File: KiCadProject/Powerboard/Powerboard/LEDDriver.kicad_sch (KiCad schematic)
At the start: 18 parts

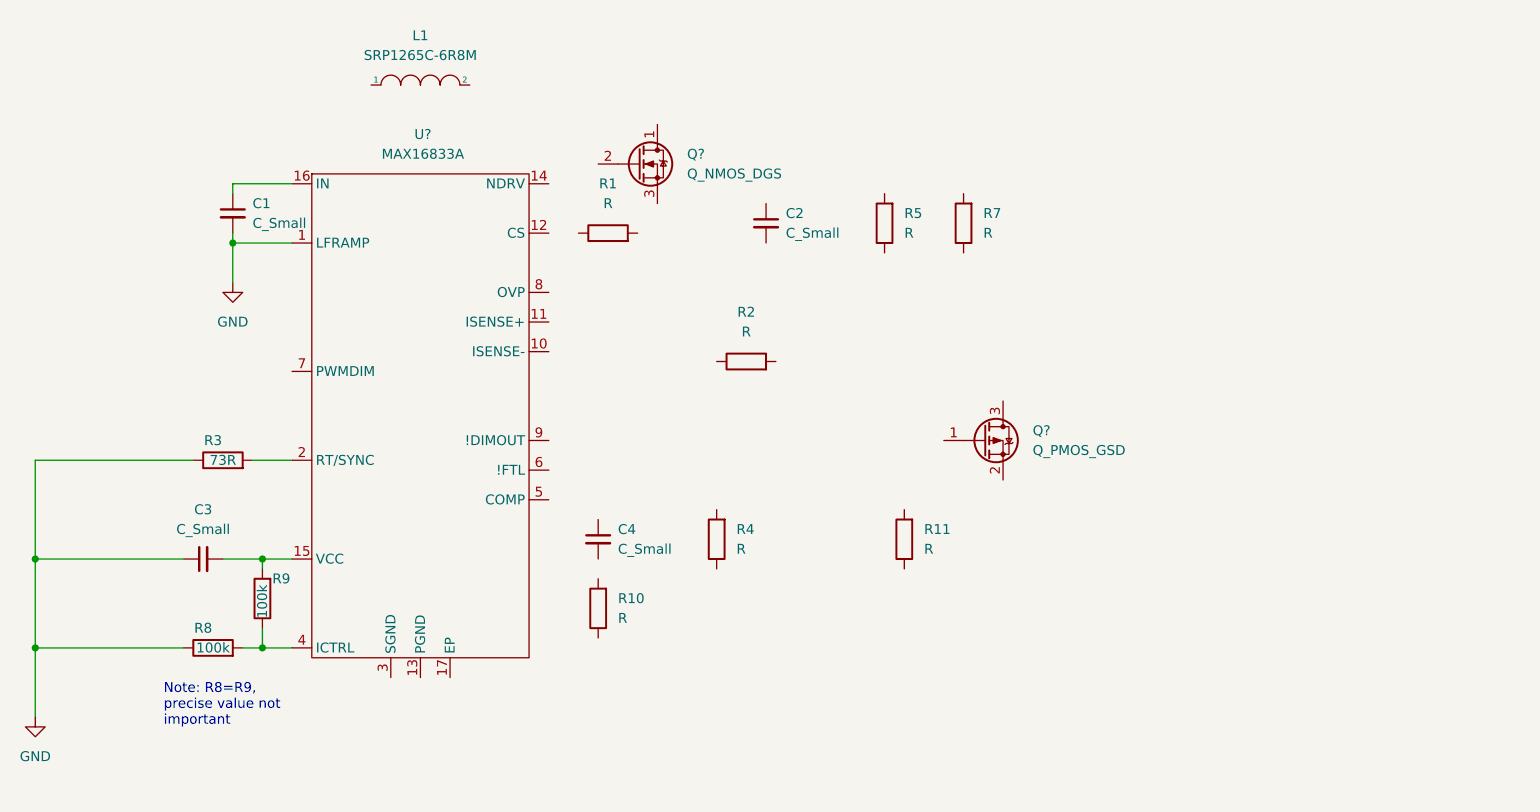
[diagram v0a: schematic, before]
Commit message: Passive components selected, only fets and diode to go
Signed-off-by: Eldalote.Electronics <Eldalote.Electronics@gmail.com>
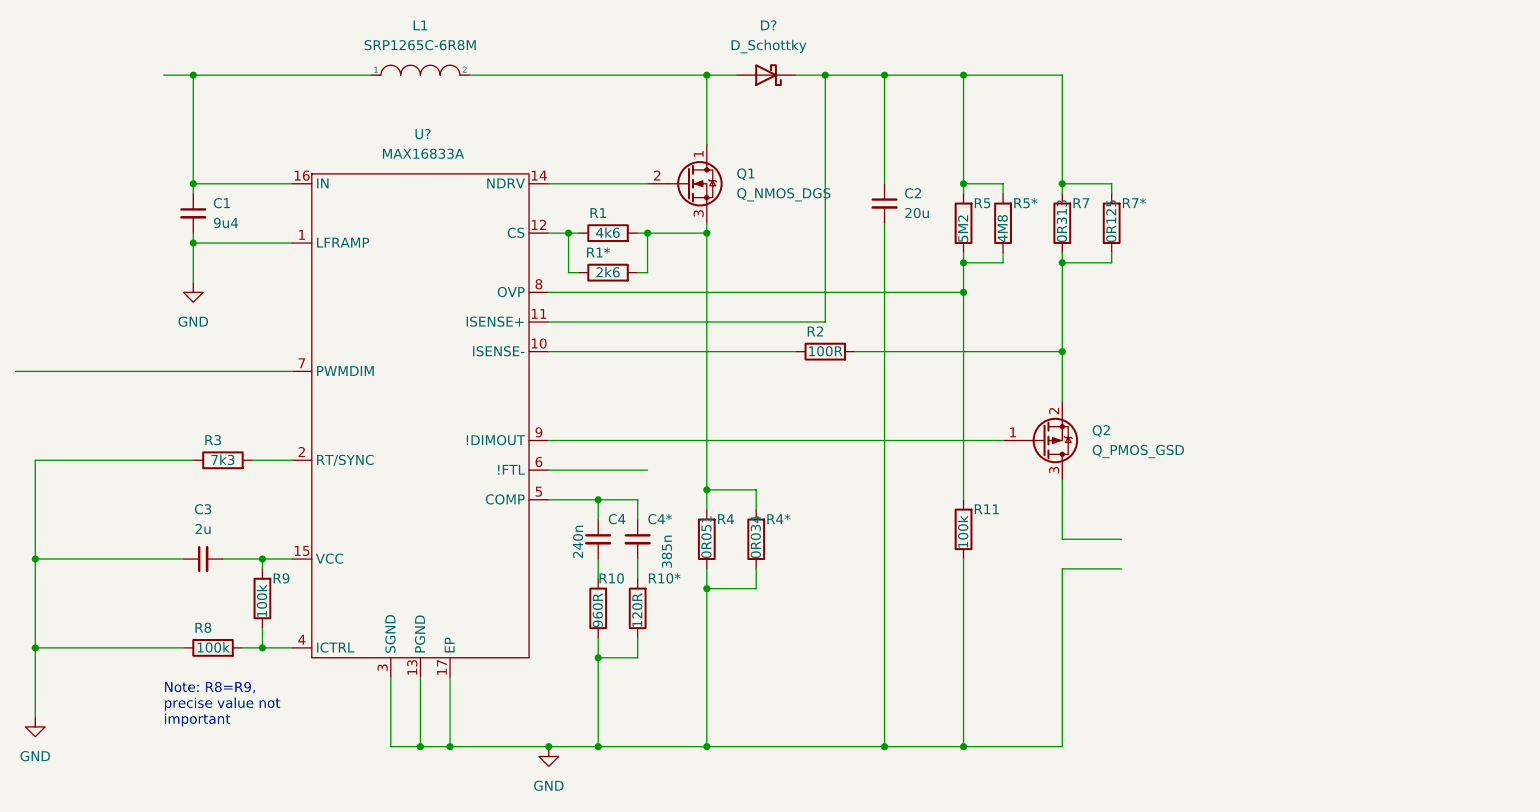
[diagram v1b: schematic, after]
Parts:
- added C4*: 385n, symbol Device:C_Small
- added D?: D_Schottky, symbol Device:D_Schottky
- added R1*: 2k6, symbol Device:R
- added R10*: 120R, symbol Device:R
- added R4*: 0R034, symbol Device:R
- added R5*: 4M8, symbol Device:R
- added R7*: 0R125, symbol Device:R
- C1: value C_Small -> 9u4
- C2: value C_Small -> 20u
- C3: value C_Small -> 2u
- C4: value C_Small -> 240n
- R1: value R -> 4k6
- R10: value R -> 960R
- R11: value R -> 100k
- R2: value R -> 100R
- R3: value 73R -> 7k3
- R4: value R -> 0R051
- R5: value R -> 5M2
- R7: value R -> 0R313
- gave numbers to parts that had none: 2
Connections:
- net GND: now also C2.2, R10.1, R11.1, R4.1, U?.13 (PGND), U?.17 (EP), U?.3 (SGND), R10*.1, R4*.1
- net at U?.10 (ISENSE-): now also R2.1
- net at U?.11 (ISENSE+): now also C2.1, R5.2, R7.2, D?.1 (K), R5*.2, R7*.2
- net at U?.12 (CS): now also R1.1, R1*.1
- net at U?.14 (NDRV): now also Q1.2 (G)
- net at C1.1, U?.16 (IN): now also L1.1
- net at U?.5 (COMP): now also C4.1, C4*.1
- net at U?.8 (OVP): now also R11.2, R5.1, R5*.1
- net at U?.9 (!DIMOUT): now also Q2.1 (G)
- net at Q2.2 (S): now also R2.2, R7.1, R7*.1
- net at R10.2: now also C4.2
- net at Q1.1 (D): now also L1.2, D?.2 (A)
- net at Q1.3 (S): now also R1.2, R4.2, R1*.2, R4*.2
- new net: C4*.2, R10*.2
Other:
- moved on the sheet: C1, C2, L1, Q1, Q2, R11, R2, R4, R5, R7

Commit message: Component selection for max16833 done?
Signed-off-by: Eldalote.Electronics <Eldalote.Electronics@gmail.com>
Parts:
- removed C4*: 385n, symbol Device:C_Small
- removed Q1: Q_NMOS_DGS, symbol Device:Q_NMOS_DGS
- removed Q2: Q_PMOS_GSD, symbol Device:Q_PMOS_GSD
- removed R1*: 2k6, symbol Device:R
- removed R10*: 120R, symbol Device:R
- removed R4*: 0R034, symbol Device:R
- removed R5*: 4M8, symbol Device:R
- removed R7*: 0R125, symbol Device:R
- added C2-2, C2-3, C2-4: 4u7, Capacitor_SMD:C_1206_3216Metric, symbol Device:C_Small
- added Q1: SIR696DP-T1-GE3, Ultralibrarianfootprints:SIR696DP-T1-GE3, symbol 2022-11-21_10-21-02:SIR696DP-T1-GE3
- added Q2: SUD50P10-43L-GE3, Package_TO_SOT_SMD:TO-252-2, symbol Device:Q_PMOS_GDS
- C1: value 9u4 -> 10u; footprint (none) -> Capacitor_SMD:C_1206_3216Metric; mfid (none) -> UMK325AB7106MMHP
- C2-1: renamed from C2; value 20u -> 4u7; footprint (none) -> Capacitor_SMD:C_1206_3216Metric
- C3: value 2u -> 2u2; footprint (none) -> Capacitor_SMD:C_0603_1608Metric
- C4: value 240n -> 220n/390n; footprint (none) -> Capacitor_SMD:C_0805_2012Metric
- D1: renamed from D?; footprint (none) -> Diode_SMD:D_PowerDI-5
- L1: footprint (none) -> Eldalote-footprints:SRP-1265C
- R1: value 4k6 -> 4k7/2k7; footprint (none) -> Resistor_SMD:R_0603_1608Metric
- R10: value 960R -> 953R/120R; footprint (none) -> Resistor_SMD:R_0402_1005Metric
- R11, R3, R8, R9: footprint (none) -> Resistor_SMD:R_0603_1608Metric
- R2: footprint (none) -> Resistor_SMD:R_0805_2012Metric
- R4: value 0R051 -> 51m/33m; footprint (none) -> Resistor_SMD:R_0603_1608Metric
- R5: value 5M2 -> 5M1/4M75; footprint (none) -> Resistor_SMD:R_0603_1608Metric
- R7: value 0R313 -> 330m/130m; footprint (none) -> Resistor_SMD:R_1206_3216Metric
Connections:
- net GND: now also C2-2.2, C2-3.2, C2-4.2
- net at C2-1.1, D1.1 (K), R5.2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: now also C2-2.1, C2-3.1, C2-4.1
- net at U?.14 (NDRV): now also Q1.4
- net at U?.9 (!DIMOUT): now also Q2.1 (G)
- net at R2.2, R7.1: now also Q2.3 (S)
- net at R1.2, R4.2: now also Q1.1, Q1.2, Q1.3
- net at D1.2 (A), L1.2: now also Q1.5, Q1.6, Q1.7, Q1.8
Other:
- moved on the sheet: C2-1

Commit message: Refinement work, and start PCB layout
Signed-off-by: Eldalote.Electronics <Eldalote.Electronics@gmail.com>
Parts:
- removed C1: 10u, Capacitor_SMD:C_1206_3216Metric, symbol Device:C_Small
- removed C2-1, C2-2, C2-3, C2-4: 4u7, Capacitor_SMD:C_1206_3216Metric, symbol Device:C_Small
- removed C3: 2u2, Capacitor_SMD:C_0603_1608Metric, symbol Device:C_Small
- removed C4: 220n/390n, Capacitor_SMD:C_0805_2012Metric, symbol Device:C_Small
- removed D1: D_Schottky, Diode_SMD:D_PowerDI-5, symbol Device:D_Schottky
- removed L1: SRP1265C-6R8M, Eldalote-footprints:SRP-1265C, symbol pspice:INDUCTOR
- removed Q1: SIR696DP-T1-GE3, Ultralibrarianfootprints:SIR696DP-T1-GE3, symbol 2022-11-21_10-21-02:SIR696DP-T1-GE3
- removed Q2: SUD50P10-43L-GE3, Package_TO_SOT_SMD:TO-252-2, symbol Device:Q_PMOS_GDS
- removed R1: 4k7/2k7, Resistor_SMD:R_0603_1608Metric, symbol Device:R
- removed R10: 953R/120R, Resistor_SMD:R_0402_1005Metric, symbol Device:R
- removed R11, R8, R9: 100k, Resistor_SMD:R_0603_1608Metric, symbol Device:R
- removed R2: 100R, Resistor_SMD:R_0805_2012Metric, symbol Device:R
- removed R3: 7k3, Resistor_SMD:R_0603_1608Metric, symbol Device:R
- removed R4: 51m/33m, Resistor_SMD:R_0603_1608Metric, symbol Device:R
- removed R5: 5M1/4M75, Resistor_SMD:R_0603_1608Metric, symbol Device:R
- removed R7: 330m/130m, Resistor_SMD:R_1206_3216Metric, symbol Device:R
- removed U?: MAX16833A, Package_SO:HTSSOP-16-1EP_4.4x5mm_P0.65mm_EP3.4x5mm_Mask2.46x2.31mm_ThermalVias, symbol Eldalote_symbols:MAX16833A
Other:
- note removed: "Note: R8=R9, precise value not important"
